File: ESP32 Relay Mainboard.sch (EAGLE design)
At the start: 84 parts, among them J1 AUDIO_JACK_TRRSSMD_RA, J2 AUDIO_JACK_TRRSSMD_RA, J3 AUDIO_JACK_TRRSSMD_RA, J4 AUDIO_JACK_TRRSSMD_RA, J5 AUDIO_JACK_TRRSSMD_RA, J6 AUDIO_JACK_TRRSSMD_RA, K1 SRD-05VDC-SL-C, K2 SRD-05VDC-SL-C, K3 SRD-05VDC-SL-C, K4 SRD-05VDC-SL-C, K5 SRD-05VDC-SL-C, K6 SRD-05VDC-SL-C, U1 ESP32-S2-WROOM, U4 LM2576SX-5.0/NOPB

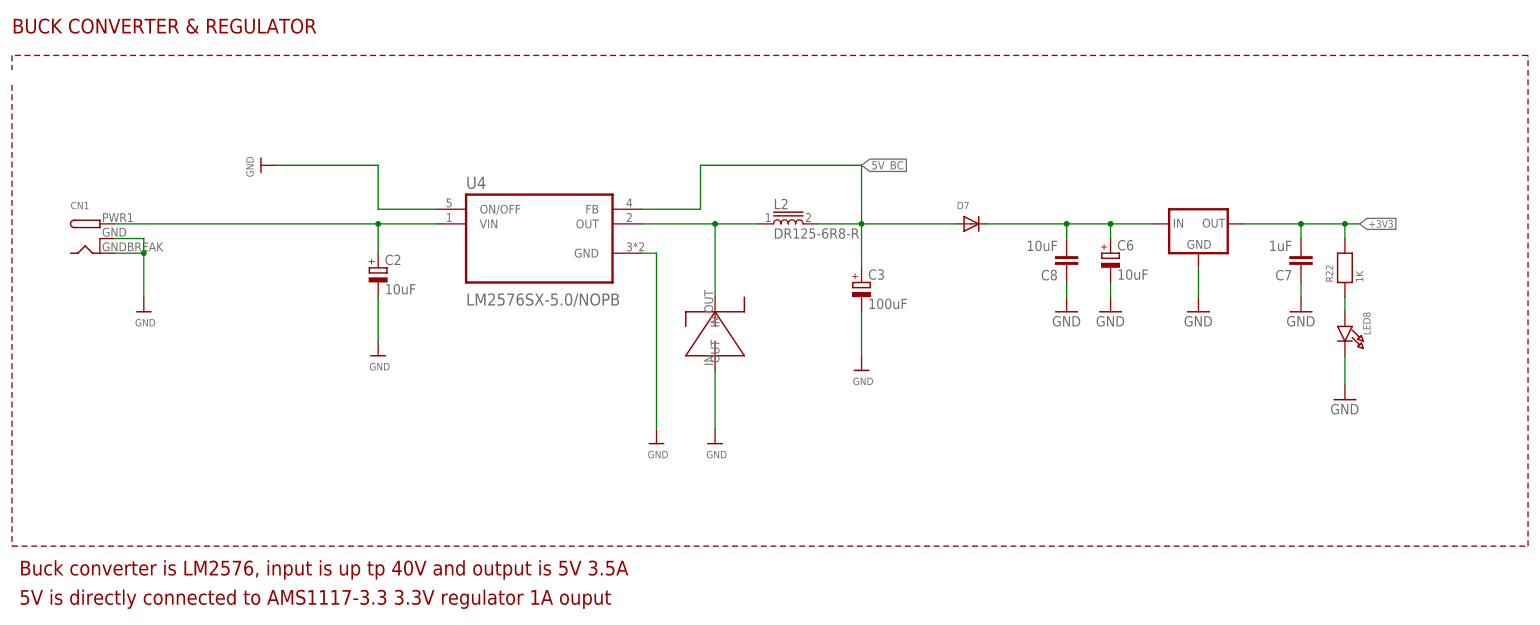
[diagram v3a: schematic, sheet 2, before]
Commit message: Add files via upload
Added SMD Varistor. Minor changes. Chnaged capacitor values to 1000uf on step down converter and 100uf on 3.3v regulator
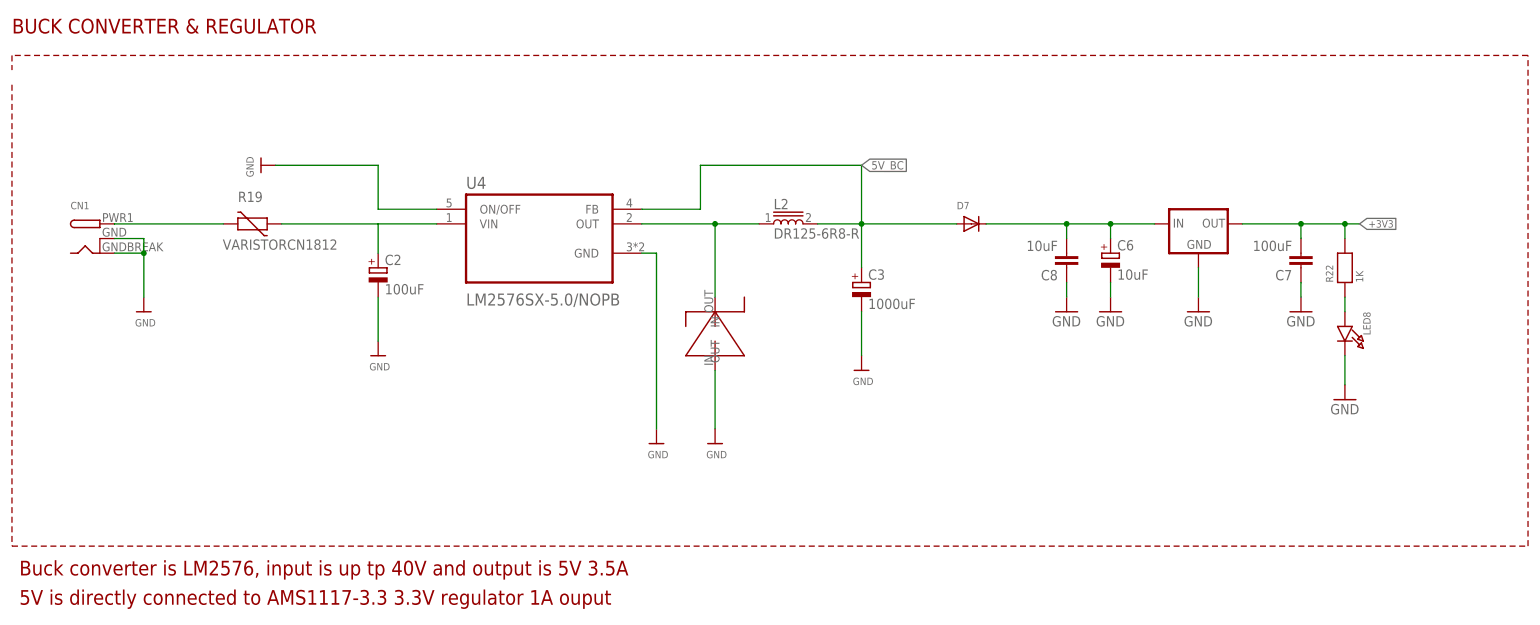
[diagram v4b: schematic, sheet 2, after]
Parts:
- added R19: VARISTORCN1812, varistor:VARISTORCN1812
- C2: value 10uF -> 100uF
- C3: value 100uF -> 1000uF
- C7: value 1uF -> 100uF
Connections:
- new net N$54: CN1.PWR, R19.2
- net N$1: now also R19.1; no longer CN1.PWR
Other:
- note added: "TVS Diode Array"
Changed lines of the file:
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@@
 <setting verticaltext="up"/>
 </settings>
-<grid distance="1" unitdist="mm" unit="mm" style="lines" multiple="1" display="no" altdistance="0.01" altunitdist="inch" altunit="inch"/>
+<grid distance="0.375" unitdist="mm" unit="mm" style="lines" multiple="1" display="no" altdistance="0.01" altunitdist="inch" altunit="inch"/>
 <layers>
 <layer number="1" name="Top" color="4" fill="1" visible="no" active="no"/>
@@
 <part name="U$9" library="microbuilder" deviceset="GND" device=""/>
 <part name="U$10" library="microbuilder" deviceset="GND" device=""/>
-<part name="C7" library="SparkFun-Capacitors" library_urn="urn:adsk.eagle:library:510" deviceset="22UF" device="-0805-6.3V-20%" package3d_urn="urn:adsk.eagle:package:37429/1" value="1uF"/>
+<part name="C7" library="SparkFun-Capacitors" library_urn="urn:adsk.eagle:library:510" deviceset="22UF" device="-0805-6.3V-20%" package3d_urn="urn:adsk.eagle:package:37429/1" value="100uF"/>
 <part name="GND6" library="supply1" library_urn="urn:adsk.eagle:library:371" deviceset="GND" device=""/>
 <part name="GND10" library="supply1" library_urn="urn:adsk.eagle:library:371" deviceset="GND" device=""/>
@@
 <part name="U$2" library="microbuilder" deviceset="GND" device=""/>
 <part name="U$4" library="microbuilder" deviceset="GND" device=""/>
-<part name="C3" library="rcl" library_urn="urn:adsk.eagle:library:334" deviceset="CPOL-EU" device="UD-10X10" package3d_urn="urn:adsk.eagle:package:23469/1" value="100uF"/>
-<part name="C2" library="rcl" library_urn="urn:adsk.eagle:library:334" deviceset="CPOL-EU" device="UD-8X10" package3d_urn="urn:adsk.eagle:package:23473/1" value="10uF"/>
+<part name="C3" library="rcl" library_urn="urn:adsk.eagle:library:334" deviceset="CPOL-EU" device="UD-10X10" package3d_urn="urn:adsk.eagle:package:23469/1" value="1000uF"/>
+<part name="C2" library="rcl" library_urn="urn:adsk.eagle:library:334" deviceset="CPOL-EU" device="UD-8X10" package3d_urn="urn:adsk.eagle:package:23473/1" value="100uF"/>
 <part name="U$7" library="microbuilder" deviceset="GND" device=""/>
 <part name="D7" library="adafruit" library_urn="urn:adsk.eagle:library:420" deviceset="DIODE" device="SMA" package3d_urn="urn:adsk.eagle:package:6240747/1"/>
@@
 <part name="D6" library="adafruit" library_urn="urn:adsk.eagle:library:420" deviceset="DIODE" device="SMA" package3d_urn="urn:adsk.eagle:package:6240747/1"/>
 <part name="U$24" library="microbuilder" deviceset="GND" device=""/>
+<part name="R19" library="varistor" library_urn="urn:adsk.eagle:library:410" deviceset="VARISTOR" device="CN1812" package3d_urn="urn:adsk.eagle:package:30610/1" value="VARISTORCN1812"/>
 </parts>
 <sheets>
@@
 <attribute name="VALUE" x="190.5" y="38.1" size="1.778" layer="96"/>
 </instance>
+<instance part="R19" gate="G$1" x="44.25" y="55.875" smashed="yes">
+<attribute name="NAME" x="41.71" y="59.685" size="1.778" layer="95"/>
+<attribute name="VALUE" x="39.085" y="51.4" size="1.778" layer="96"/>
+</instance>
 </instances>
 <busses>
@@
 <net name="N$1" class="0">
 <segment>
-<pinref part="CN1" gate="G$1" pin="PWR"/>
-<wire x1="20.32" y1="55.88" x2="66.04" y2="55.88" width="0.1524" layer="91"/>
 <pinref part="U4" gate="G$1" pin="VIN"/>
 <pinref part="C2" gate="G$1" pin="+"/>
 <wire x1="66.04" y1="55.88" x2="76.2" y2="55.88" width="0.1524" layer="91"/>
-<wire x1="66.04" y1="50.8" x2="66.04" y2="55.88" width="0.1524" layer="91"/>
-<junction x="66.04" y="55.88"/>
+<wire x1="66.04" y1="50.8" x2="66.04" y2="55.869" width="0.1524" layer="91"/>
+<pinref part="R19" gate="G$1" pin="1"/>
+<wire x1="66.04" y1="55.875" x2="66.04" y2="55.88" width="0.1524" layer="91"/>
+<wire x1="66.04" y1="55.875" x2="49.33" y2="55.875" width="0.1524" layer="91"/>
+<wire x1="66.04" y1="55.869" x2="66.04" y2="55.875" width="0.1524" layer="91"/>
 </segment>
 </net>
@@
 <wire x1="193.04" y1="53.34" x2="193.04" y2="55.88" width="0.1524" layer="91"/>
 <junction x="193.04" y="55.88"/>
+</segment>
+</net>
+<net name="N$54" class="0">
+<segment>
+<pinref part="CN1" gate="G$1" pin="PWR"/>
+<pinref part="R19" gate="G$1" pin="2"/>
+<wire x1="20.32" y1="55.88" x2="20.32" y2="55.875" width="0.1524" layer="91"/>
+<wire x1="20.32" y1="55.875" x2="39.17" y2="55.875" width="0.1524" layer="91"/>
 </segment>
 </net>
@@
 <text x="161.29" y="62.23" size="2.54" layer="94" font="vector" ratio="13">reduce parasitic drain.</text>
 <text x="161.29" y="49.53" size="2.54" layer="94" font="vector" ratio="13">Two 5.1K resistors for USB-C connection detection.</text>
+<text x="110.29" y="17.53" size="2.54" layer="94" font="vector" ratio="13">TVS Diode Array</text>
 </plain>
 <instances>
